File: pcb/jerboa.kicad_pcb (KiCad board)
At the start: 2 copper layers, 50 x 118.1 mm, 93 parts, among them IC1 SL18860DC, IC2 MAX-M8Q, IC3 Si4460, J1 CONN_01x02, J2 CONN_01x03, J3 CONN_01x02, J4 CONN_01x02, P1 SWD_TC, P2 144MHz, P3 434MHz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

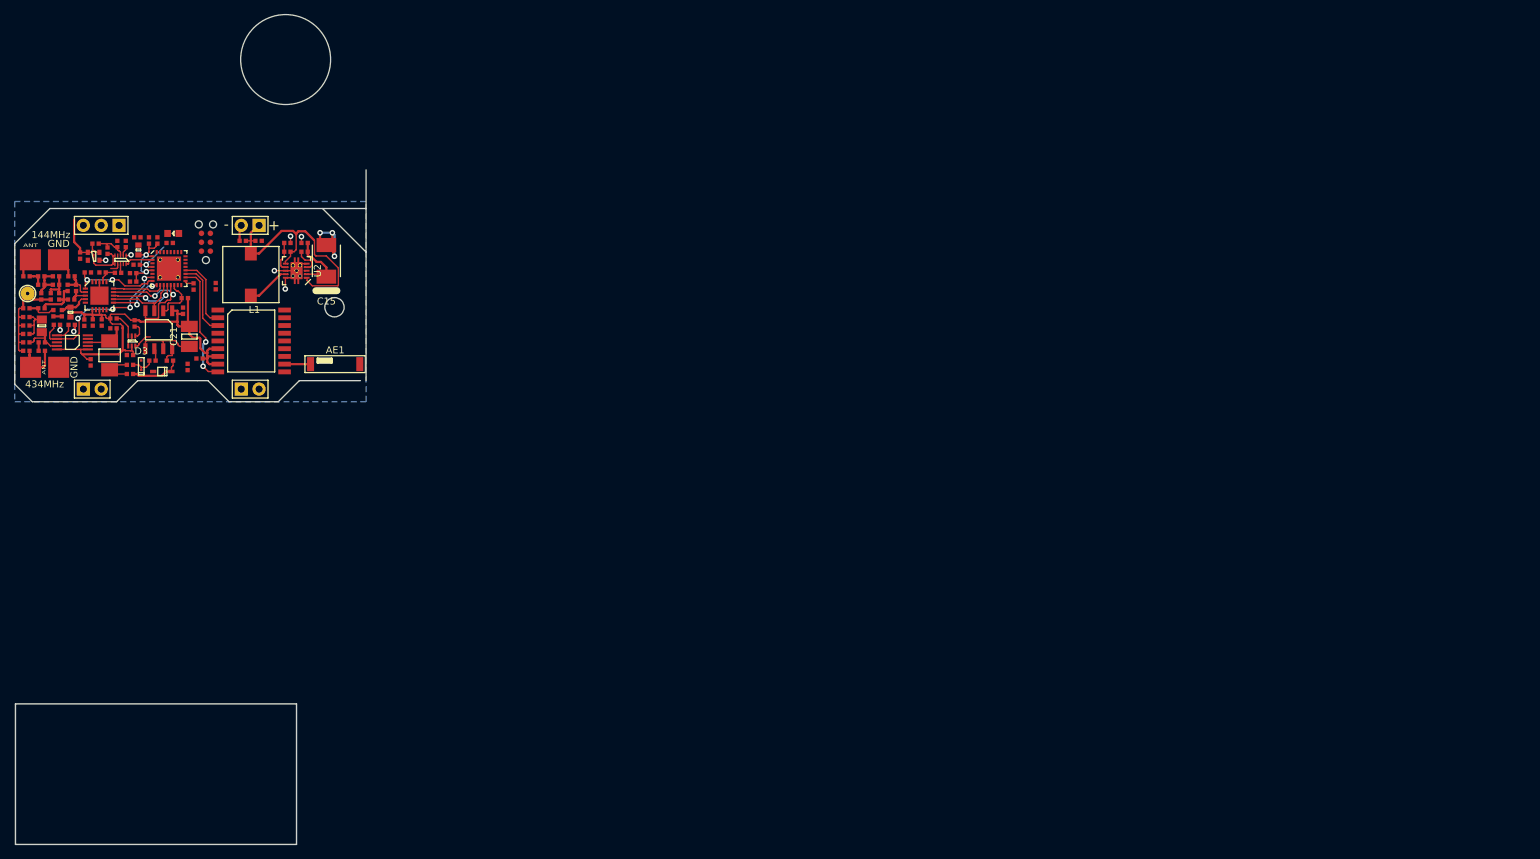
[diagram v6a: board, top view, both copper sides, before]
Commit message: Schematic (and some pcb) using si4460 for both 144MHz and 434MHz
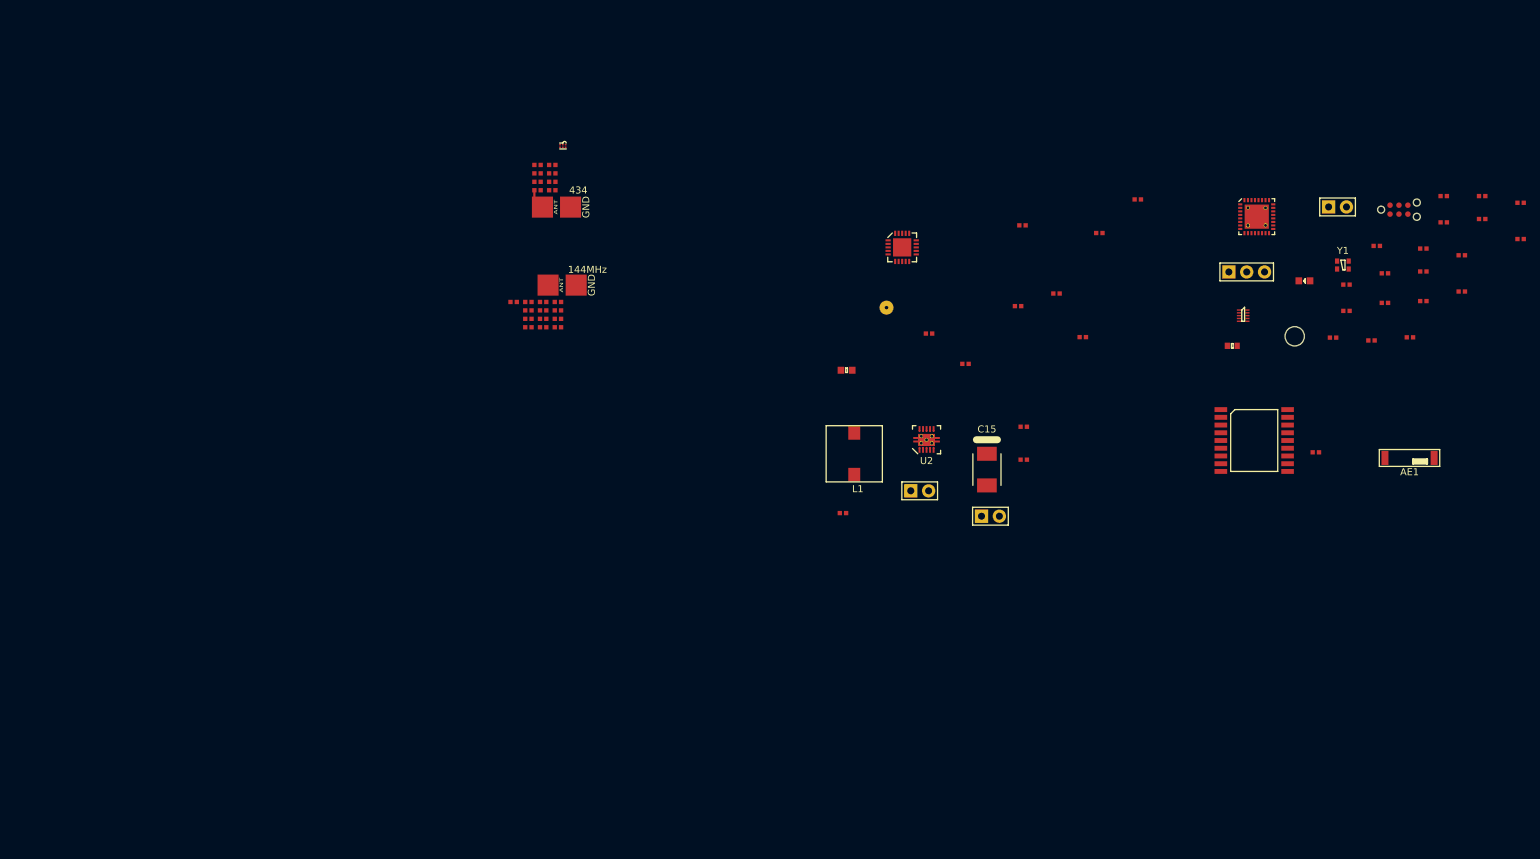
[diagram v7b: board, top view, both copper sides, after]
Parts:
- removed C0: 39pF, agg:0402
- removed CC2: 470pF, agg:0402
- removed CM1: 6.8pF, agg:0402
- removed CM2, CM3: 18pF, agg:0402
- removed CP1: 3pF, agg:0402
- removed CP2: 2pF, agg:0402
- removed CR1: 12pF, agg:0402
- removed CR2: 6.2pF, agg:0402
- removed L0: 22nH, agg:0402
- removed LM1: 56nH, agg:0402
- removed LM2, LM4: 47nH, agg:0402
- removed LM3: 68nH, agg:0402
- removed LR1: 220nH, agg:0402
- removed LR2: 150nH, agg:0402
- removed Lchoke1: 470nH, agg:0603-L
- removed R10: 604k, agg:0402
- removed R11: 499k, agg:0402
- removed R12, R14, R15: 1M, agg:0402
- removed R13: 10k, agg:0402
- removed R16: 4k7, agg:0402
- removed R17, R18: 100k, agg:0402
- removed U4: TMP102, agg:SOT-666
- removed U5: MICRF112YMM, agg:MSOP-10
- removed Y2: 13.56MHz, agg:XTAL-50x32
- added C33: 470pF, agg:0402, F.Cu at (111.8, 87.8)
- added L10: 18nH, agg:0402, F.Cu at (108.9, 70.7)
- added L11: 68nH, agg:0402, F.Cu at (109.7, 90.2)
- added L12: 47nH, agg:0402, F.Cu at (111.8, 89.0)
- added L4: 56nH, agg:0402, F.Cu at (108.9, 68.3)
- added L5: 150nH, agg:0402, F.Cu at (182.8, 86.6)
- added L6: 22nH, agg:0402, F.Cu at (107.6, 87.8)
- added L7: 18nH, agg:0402, F.Cu at (111.0, 69.5)
- added L8: 56nH, agg:0402, F.Cu at (107.6, 90.2)
- added L9: 47nH, agg:0402, F.Cu at (107.6, 91.4)
- C20: value 100nF -> 10nF
- C21: value 10uF -> 18pF; footprint Jerboa:1411 -> agg:0402
- C22: value 36pF -> 12pF
- C23: value 12pF -> 39pF
- C24: value 18pF -> 6.2pF
- C25: value 10nF -> 8.2pF
- C26: value 100nF -> 6.8pF
- C27: value 1.2pF -> 15pF
- C28: value 2.2pF -> 18pF
- C29: value 100nF -> 3pF
- C30: value 6.8pF -> 8.2pF
- C31: value 100nF -> 18pF
- C32: value 100nF -> 2pF
- D2: value D_Capacitance -> ESD_DIODE; footprint agg:SOD-323 -> agg:0402
- D3: value D_Capacitance -> ESD_DIODE; footprint Jerboa:SC-79 -> agg:0402
- L2: value 680nH -> 390nH; footprint agg:0805 -> agg:0603
- L3: value 43nH -> 220nH
- P2: value 144MHz -> 434
- P3: value 434MHz -> 144MHz
- U3: value MCP4812 -> BGS12PL6E6327XTSA1; footprint agg:SOIC-8 -> Jerboa:DFN-6-infineon
- moved R5 196.5 mm to (243.3, 76.0), turned to 0 degrees
- moved R4 194.4 mm to (243.3, 72.7), turned to 0 degrees
- moved C6 194.1 mm to (248.8, 73.7), turned to 0 degrees
- moved C2 191.9 mm to (237.9, 76.5)
- moved C9 189.0 mm to (248.8, 78.8), turned to 0 degrees
- moved R2 188.9 mm to (237.9, 72.7), turned to 0 degrees
- moved C10 188.6 mm to (240.4, 86.3), turned to 0 degrees
- moved C4 188.5 mm to (240.4, 81.2), turned to 0 degrees
- moved R1 187.3 mm to (235.0, 83.5), turned to 0 degrees
- moved C1 185.7 mm to (229.5, 83.7), turned to 0 degrees
- moved C8 183.6 mm to (235.0, 87.7)
- moved R9 183.5 mm to (228.3, 79.8)
- moved J1 179.1 mm to (222.8, 74.3)
- moved R7 178.0 mm to (229.5, 87.9), turned to 0 degrees
- moved C3 177.8 mm to (227.6, 93.3), turned to 0 degrees
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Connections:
- C20 pad 1: 3v3 -> Net-(C20-Pad1)
- C20 pad 2: GND -> Net-(C20-Pad2)
- C21 pad 1: 3v3 -> /radio/RADIO_TX_434
- C21 pad 2: GND -> Net-(C21-Pad2)
- C22 pad 1: Net-(C22-Pad1) -> /radio/RADIO_RXp
- C22 pad 2: Net-(C22-Pad2) -> GND
- C23 pad 1: Net-(C23-Pad1) -> /radio/RADIO_TX_144
- C23 pad 2: Net-(C22-Pad2) -> Net-(C23-Pad2)
- C24 pad 1: Net-(C24-Pad1) -> /radio/RADIO_RXn
- C24 pad 2: GND -> Net-(C24-Pad2)
- C25 pad 1: 3v3 -> Net-(C25-Pad1)
- C26 pad 1: GND -> Net-(C26-Pad1)
- C26 pad 2: 3v3 -> GND
- C27 pad 1: GND -> Net-(C27-Pad1)
- C27 pad 2: Net-(C27-Pad2) -> GND
- C28 pad 1: Net-(C27-Pad2) -> Net-(C28-Pad1)
- C28 pad 2: Net-(C28-Pad2) -> GND
- C29 pad 1: Net-(C29-Pad1) -> Net-(C28-Pad1)
- C29 pad 2: GND -> Net-(C29-Pad2)
- C31 pad 1: Net-(C29-Pad1) -> Net-(C29-Pad2)
- C32 pad 1: Net-(C29-Pad1) -> Net-(C29-Pad2)
- C32 pad 2: GND -> Net-(C32-Pad2)
- D2 pad 1: Net-(C22-Pad1) -> Net-(C30-Pad1)
- D3 pad 1: Net-(C23-Pad1) -> Net-(C33-Pad2)
- IC3 pad 4: /radio/RADIO_TX -> Net-(C20-Pad1)
- J4 pad 2: GND -> /BATT_V
- L2 pad 1: Net-(C29-Pad1) -> 3v3
- L2 pad 2: Net-(C27-Pad2) -> Net-(C20-Pad1)
- L3 pad 1: Net-(C30-Pad1) -> /radio/RADIO_RXn
- L3 pad 2: Net-(C28-Pad2) -> /radio/RADIO_RXp
- P2 pad 1: Net-(CC2-Pad2) -> Net-(C30-Pad1)
- P3 pad 1: Net-(C30-Pad1) -> Net-(C33-Pad2)
- U1 pad 14: /DAC_NCS -> /BATT_V
- U1 pad 25: /LOW_BATT -> Net-(U1-Pad25)
- U1 pad 27: /TMP_ALERT -> Net-(U1-Pad27)
- U1 pad 7: /MICRF_EN -> /FREQ_CTRL
- U2 pad 4: /LOW_BATT -> Net-(U2-Pad4)
- U2 pad 7: Net-(R10-Pad2) -> GND
- U3 pad 1: 3v3 -> /radio/RADIO_TX_434
- U3 pad 2: /DAC_NCS -> GND
- U3 pad 3: /MCU_SCK -> /radio/RADIO_TX_144
- U3 pad 4: /MCU_MOSI -> 3v3
- U3 pad 5: GND -> Net-(C20-Pad2)
- U3 pad 6: /radio/FINE -> /FREQ_CTRL
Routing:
- net 3v3: track 101.5 -> 0.00 mm, vias 2 -> 0
- net GND: track 59.1 -> 0.00 mm, vias 11 -> 0
- net Net-(C12-Pad1): track 36.2 -> 0.00 mm
- net /MICRF_EN: track 23.2 -> 0.00 mm, vias 4 -> 0
- net /MCU_MOSI: track 18.7 -> 0.00 mm, vias 2 -> 0
- net /GPS_~RESET: track 17.0 -> 0.00 mm, vias 2 -> 0
- net /MCU_SHUTDOWN_TO_RADIO: track 12.6 -> 0.00 mm, vias 2 -> 0
- net /TX_GPS_from_MCU: track 10.8 -> 0.00 mm
- net /MCU_SCK: track 10.4 -> 0.00 mm
- net /RX_GPS_from_MCU: track 10.2 -> 0.00 mm
- net /MCU_MISO: track 9.62 -> 0.00 mm, vias 2 -> 0
- net /MCU_nIRQ_TO_RADIO: track 8.14 -> 0.00 mm, vias 2 -> 0
- net Net-(C22-Pad1): track 7.56 -> 0.00 mm
- net /SI4460_NSS: track 7.43 -> 0.00 mm
- net /DAC_NCS: track 7.02 -> 0.00 mm
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- removed copper zone on B.Cu, net GND
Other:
- board outline removed
- net class Power removed
- rule pad_to_mask_clearance: 0.2 -> 0
- board text removed: "+"
- board text removed: "-"
- board text removed: "ANT GND"

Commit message: Add footprints for 50ohm matching of antennas, work on schematic & pcb
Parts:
- moved U3 23.4 mm to (113.9, 89.0), turned to 270 degrees
- moved C21 20.1 mm to (112.3, 88.4)
- moved IC2 19.5 mm to (230.4, 108.8)
- moved C25 15.4 mm to (107.0, 84.8)
- moved L4 15.3 mm to (109.1, 83.6)
- moved L7 14.7 mm to (107.0, 83.6), turned to 180 degrees
- moved C27 12.4 mm to (107.0, 82.4), turned to 180 degrees
- moved L10 11.7 mm to (109.1, 82.4), turned to 0 degrees
- moved C30 10.1 mm to (107.0, 81.2), turned to 180 degrees
- moved D2 9.30 mm to (109.1, 81.2), turned to 180 degrees
- moved AE1 8.37 mm to (241.1, 112.1), turned to 180 degrees
- moved C31 7.92 mm to (106.0, 86.0), turned to 180 degrees
- moved P3 7.57 mm to (108.7, 92.0)
- moved C23 7.03 mm to (112.3, 89.6), turned to 180 degrees
- moved C32 6.53 mm to (106.0, 87.2), turned to 180 degrees
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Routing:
- net GND: track 0.00 -> 3.78 mm
- net Net-(C30-Pad1): track 2.88 -> 0.00 mm
- net Net-(AE1-Pad2): track 0.00 -> 2.45 mm
- net /radio/RADIO_TX_434: track 0.00 -> 1.00 mm
- net /radio/RADIO_TX_144: track 0.00 -> 1.00 mm
